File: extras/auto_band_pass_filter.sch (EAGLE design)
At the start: 31 parts, among them M1 ARDUINO-PRO-MINI-3.3V, U1 FAIRCHILD_FST3253MXFAIRCHILD_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, U2 FAIRCHILD_FST3253MXFAIRCHILD_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

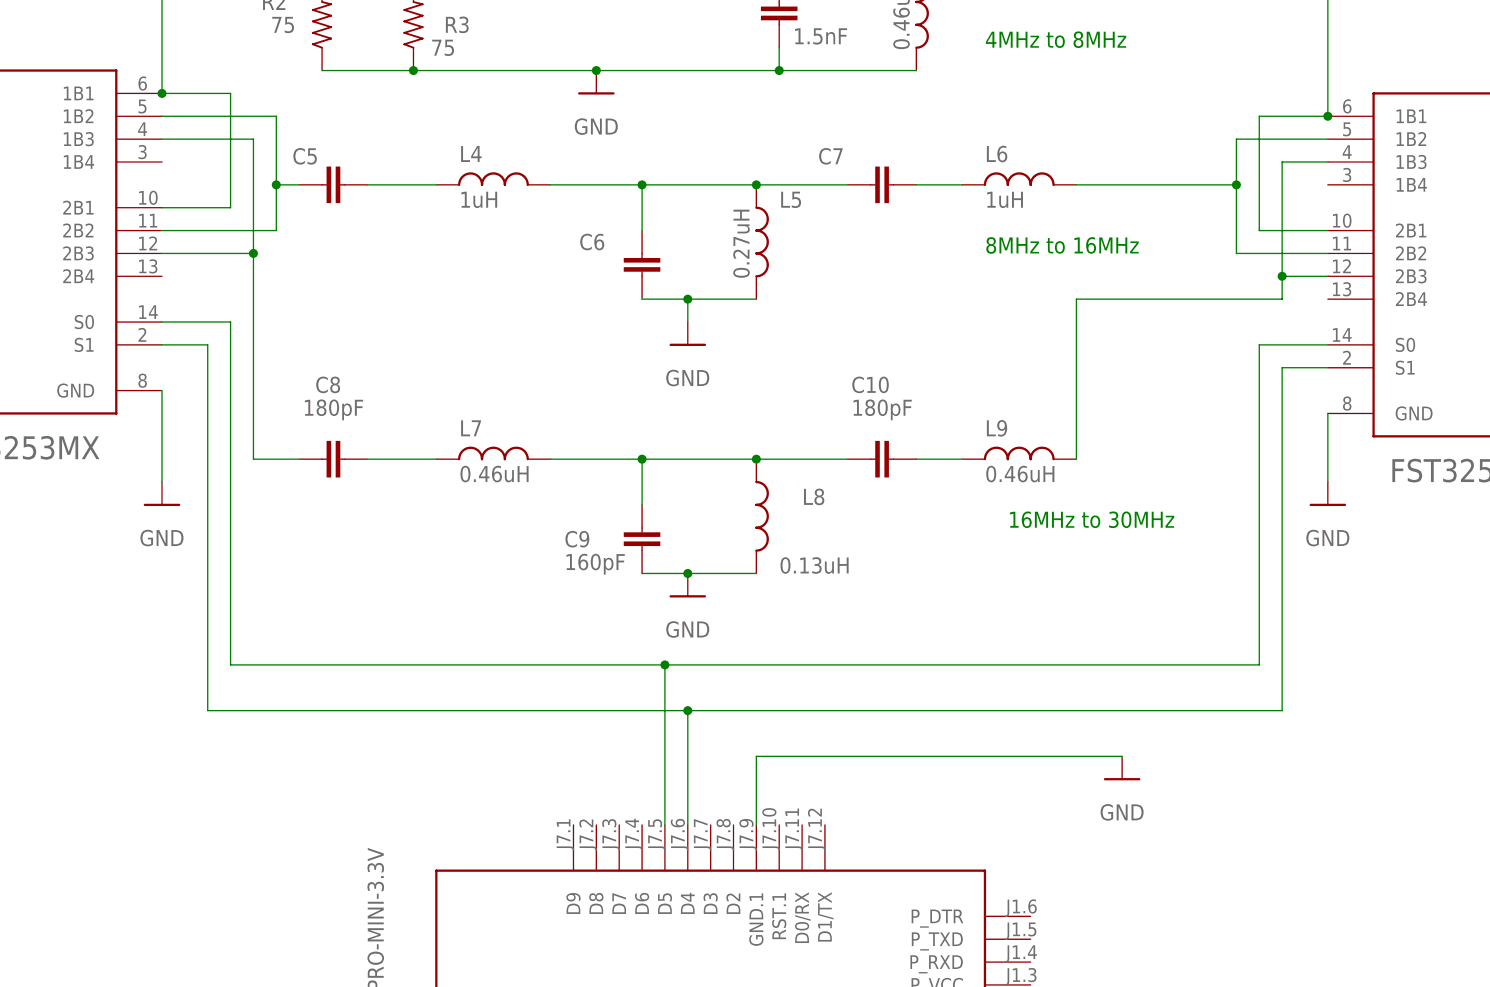
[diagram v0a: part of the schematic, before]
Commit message: Auto bandpass filter
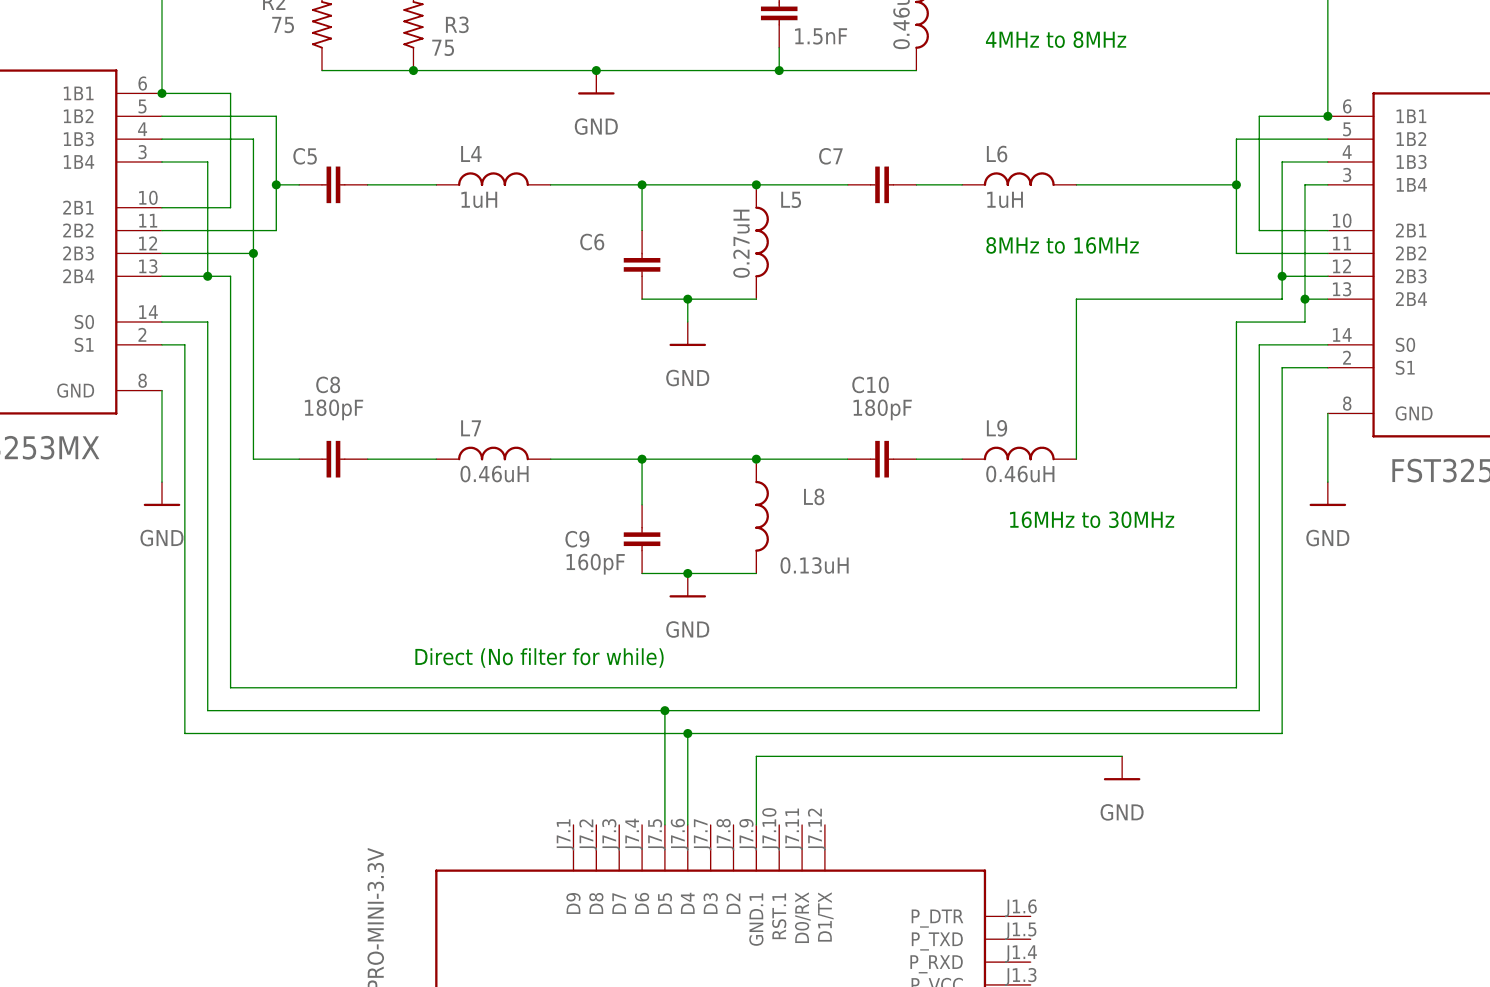
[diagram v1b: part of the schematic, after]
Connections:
- new net N$25: U1.1B4, U1.2B4, U2.1B4, U2.2B4
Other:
- note added: "Direct (No filter for while)"
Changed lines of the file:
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@@
 <text x="-139.7" y="193.04" size="1.778" layer="91">16MHz to 30MHz</text>
 <text x="-58.42" y="241.3" size="1.778" layer="91">SI4735 AMI circuit</text>
+<text x="-205.74" y="177.8" size="1.778" layer="91">Direct (No filter for while)</text>
 </plain>
 <instances>
@@
 <segment>
 <pinref part="U1" gate="G$0" pin="S0"/>
-<wire x1="-233.68" y1="215.9" x2="-226.06" y2="215.9" width="0.1524" layer="91"/>
-<wire x1="-226.06" y1="215.9" x2="-226.06" y2="177.8" width="0.1524" layer="91"/>
-<wire x1="-226.06" y1="177.8" x2="-177.8" y2="177.8" width="0.1524" layer="91"/>
-<wire x1="-177.8" y1="177.8" x2="-111.76" y2="177.8" width="0.1524" layer="91"/>
-<wire x1="-111.76" y1="177.8" x2="-111.76" y2="213.36" width="0.1524" layer="91"/>
+<wire x1="-233.68" y1="215.9" x2="-228.6" y2="215.9" width="0.1524" layer="91"/>
+<wire x1="-228.6" y1="215.9" x2="-228.6" y2="172.72" width="0.1524" layer="91"/>
+<wire x1="-228.6" y1="172.72" x2="-177.8" y2="172.72" width="0.1524" layer="91"/>
+<wire x1="-177.8" y1="172.72" x2="-111.76" y2="172.72" width="0.1524" layer="91"/>
+<wire x1="-111.76" y1="172.72" x2="-111.76" y2="213.36" width="0.1524" layer="91"/>
 <pinref part="U2" gate="G$0" pin="S0"/>
 <wire x1="-111.76" y1="213.36" x2="-104.14" y2="213.36" width="0.1524" layer="91"/>
 <pinref part="M1" gate="G$1" pin="D5"/>
-<wire x1="-177.8" y1="160.02" x2="-177.8" y2="177.8" width="0.1524" layer="91"/>
-<junction x="-177.8" y="177.8"/>
+<wire x1="-177.8" y1="160.02" x2="-177.8" y2="172.72" width="0.1524" layer="91"/>
+<junction x="-177.8" y="172.72"/>
 </segment>
 </net>
@@
 <segment>
 <pinref part="U1" gate="G$0" pin="S1"/>
-<wire x1="-233.68" y1="213.36" x2="-228.6" y2="213.36" width="0.1524" layer="91"/>
-<wire x1="-228.6" y1="213.36" x2="-228.6" y2="172.72" width="0.1524" layer="91"/>
-<wire x1="-228.6" y1="172.72" x2="-175.26" y2="172.72" width="0.1524" layer="91"/>
-<wire x1="-175.26" y1="172.72" x2="-109.22" y2="172.72" width="0.1524" layer="91"/>
-<wire x1="-109.22" y1="172.72" x2="-109.22" y2="210.82" width="0.1524" layer="91"/>
+<wire x1="-233.68" y1="213.36" x2="-231.14" y2="213.36" width="0.1524" layer="91"/>
+<wire x1="-231.14" y1="213.36" x2="-231.14" y2="170.18" width="0.1524" layer="91"/>
+<wire x1="-231.14" y1="170.18" x2="-175.26" y2="170.18" width="0.1524" layer="91"/>
+<wire x1="-175.26" y1="170.18" x2="-109.22" y2="170.18" width="0.1524" layer="91"/>
+<wire x1="-109.22" y1="170.18" x2="-109.22" y2="210.82" width="0.1524" layer="91"/>
 <pinref part="U2" gate="G$0" pin="S1"/>
 <wire x1="-109.22" y1="210.82" x2="-104.14" y2="210.82" width="0.1524" layer="91"/>
 <pinref part="M1" gate="G$1" pin="D4"/>
-<wire x1="-175.26" y1="160.02" x2="-175.26" y2="172.72" width="0.1524" layer="91"/>
-<junction x="-175.26" y="172.72"/>
+<wire x1="-175.26" y1="160.02" x2="-175.26" y2="170.18" width="0.1524" layer="91"/>
+<junction x="-175.26" y="170.18"/>
 </segment>
 </net>
@@
 </segment>
 </net>
+<net name="N$25" class="0">
+<segment>
+<pinref part="U2" gate="G$0" pin="1B4"/>
+<wire x1="-104.14" y1="231.14" x2="-106.68" y2="231.14" width="0.1524" layer="91"/>
+<wire x1="-106.68" y1="231.14" x2="-106.68" y2="218.44" width="0.1524" layer="91"/>
+<pinref part="U2" gate="G$0" pin="2B4"/>
+<wire x1="-106.68" y1="218.44" x2="-104.14" y2="218.44" width="0.1524" layer="91"/>
+<wire x1="-106.68" y1="218.44" x2="-106.68" y2="215.9" width="0.1524" layer="91"/>
+<junction x="-106.68" y="218.44"/>
+<wire x1="-106.68" y1="215.9" x2="-114.3" y2="215.9" width="0.1524" layer="91"/>
+<wire x1="-114.3" y1="215.9" x2="-114.3" y2="175.26" width="0.1524" layer="91"/>
+<wire x1="-114.3" y1="175.26" x2="-226.06" y2="175.26" width="0.1524" layer="91"/>
+<wire x1="-226.06" y1="175.26" x2="-226.06" y2="220.98" width="0.1524" layer="91"/>
+<pinref part="U1" gate="G$0" pin="1B4"/>
+<wire x1="-233.68" y1="233.68" x2="-228.6" y2="233.68" width="0.1524" layer="91"/>
+<wire x1="-228.6" y1="233.68" x2="-228.6" y2="220.98" width="0.1524" layer="91"/>
+<pinref part="U1" gate="G$0" pin="2B4"/>
+<wire x1="-228.6" y1="220.98" x2="-233.68" y2="220.98" width="0.1524" layer="91"/>
+<wire x1="-226.06" y1="220.98" x2="-228.6" y2="220.98" width="0.1524" layer="91"/>
+<junction x="-228.6" y="220.98"/>
+</segment>
+</net>

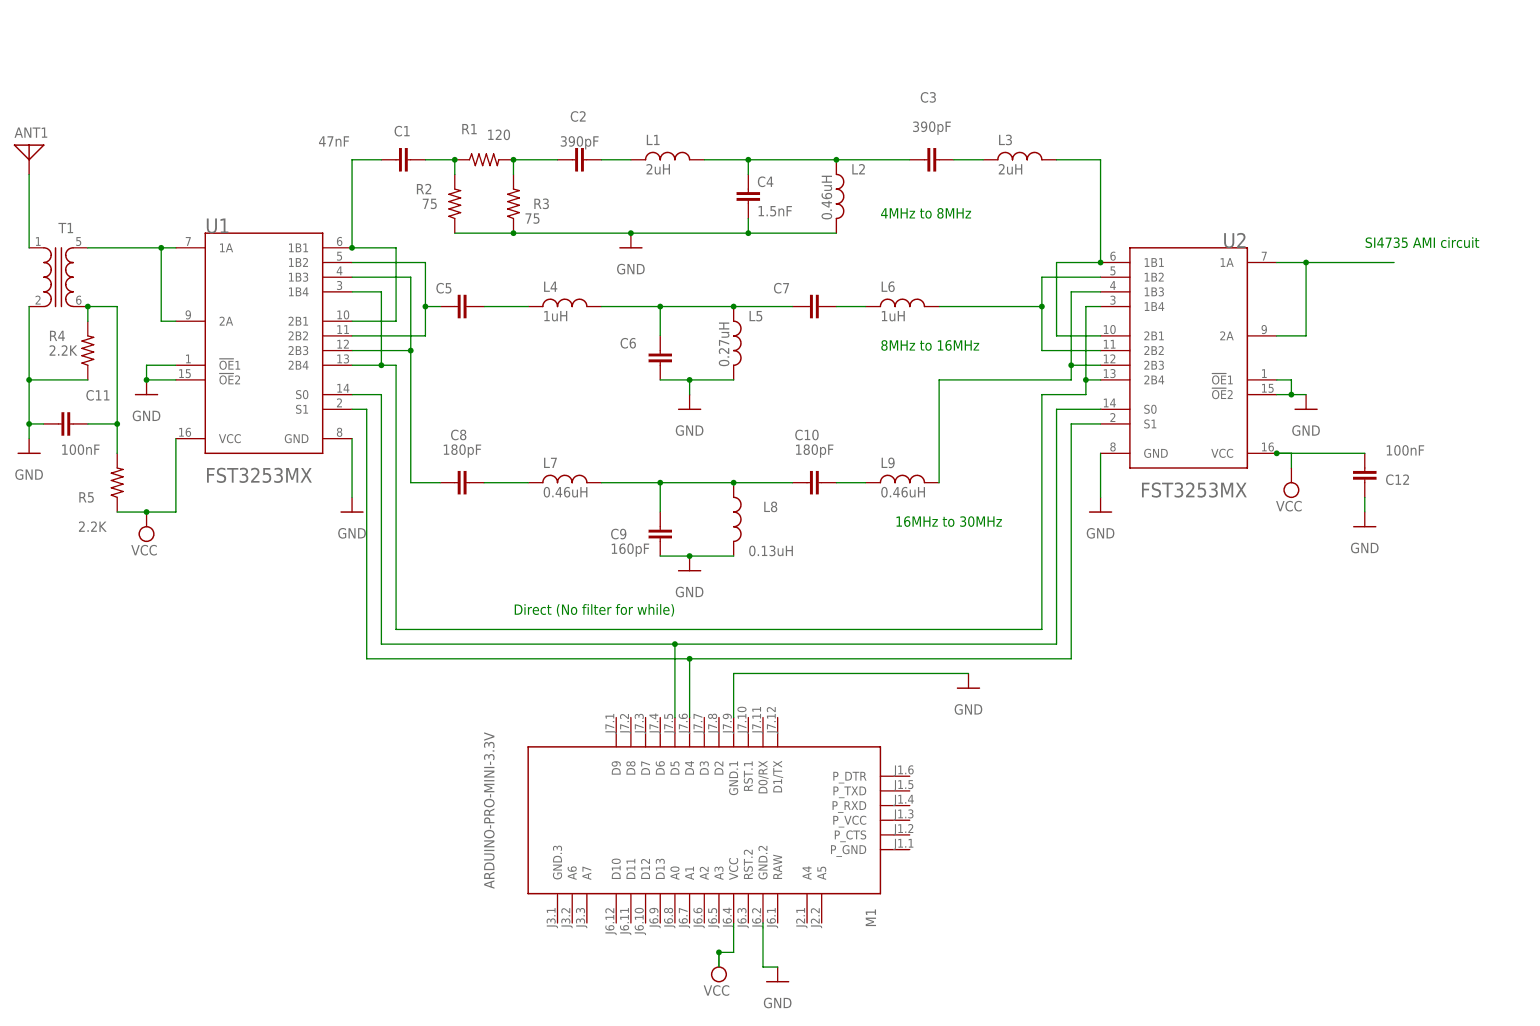
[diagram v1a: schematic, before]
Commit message: BPF controlled by Arduino
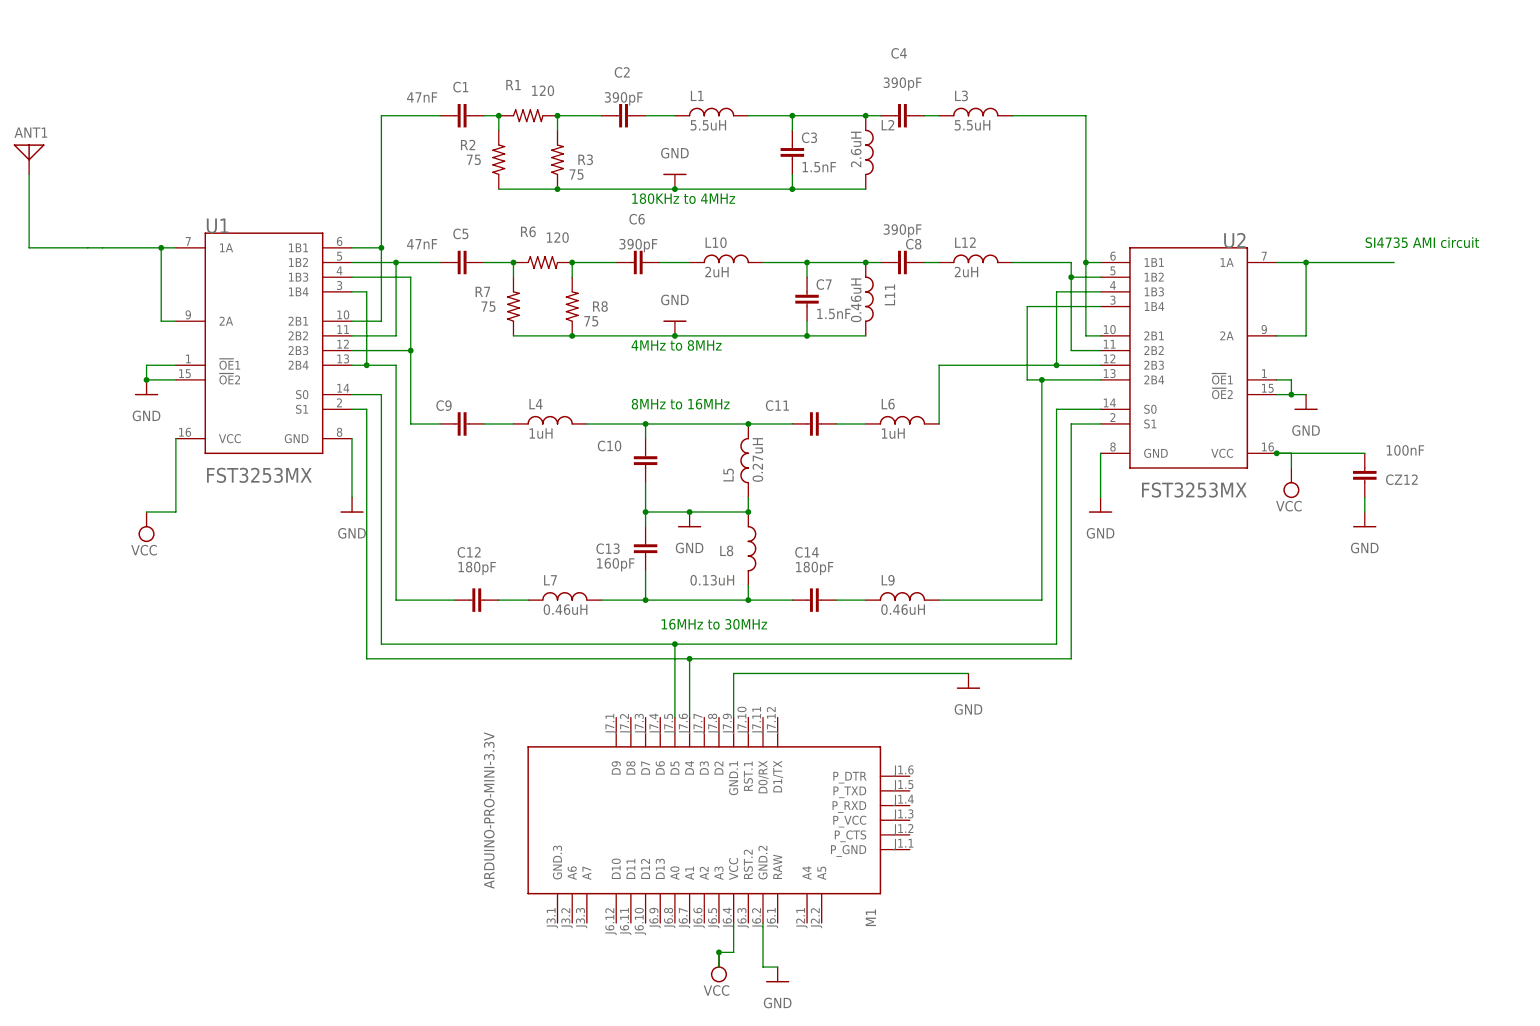
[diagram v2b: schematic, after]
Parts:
- removed R4, R5: 2.2K, Resistor:R-US_AXIAL-7.2MM-PITCH
- removed T1: (no value), special:XFORMER
- added C13: 160pF, capacitor-wima:C2,5-3
- added C14: 180pF, capacitor-wima:C2,5-3
- added CZ12: 100nF, capacitor-wima:C2,5-3
- added L10, L12: 2uH, ngspice-simulation:L
- added L11: 0.46uH, ngspice-simulation:L
- added R6: 120, Resistor:R-US_AXIAL-7.2MM-PITCH
- added R7, R8: 75, Resistor:R-US_AXIAL-7.2MM-PITCH
- C10: value 180pF -> (none)
- C11: value 100nF -> (none)
- C12: value 100nF -> 180pF
- C3: value 390pF -> 1.5nF
- C4: value 1.5nF -> 390pF
- C5: value (none) -> 47nF
- C6: value (none) -> 390pF
- C7: value (none) -> 1.5nF
- C8: value 180pF -> 390pF
- C9: value 160pF -> (none)
- L1, L3: value 2uH -> 5.5uH
- L2: value 0.46uH -> 2.6uH
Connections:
- removed net N$25: U1.1B4, U1.2B4, U2.1B4, U2.2B4
- new net N$13: C7.1, C8.1, L10.2, L11.1
- new net N$26: C6.2, L10.1
- new net N$27: L6.2, U2.1B3, U2.2B3
- new net N$28: C8.2, L12.1
- new net N$29: L9.2, U2.1B4, U2.2B4
- net GND: now also C10.1, C13.1, C3.2, C7.2, CZ12.1, L11.2, L5.1, L8.1, R7.1, R8.1; no longer C11.1, C12.1, C4.2, C6.1, C9.2, L5.2, L8.2, R4.1, T1T1.P2
- net N$10: now also C12.2; no longer C8.2
- net N$11: now also C4.2; no longer C3.2
- net N$12: now also C11.2; no longer C7.2
- net N$14: now also C9.1, U1.1B3, U1.2B3; no longer L6.2, U2.1B2, U2.2B2
- net N$16: now also C14.2; no longer C10.2
- net N$17: now also C5.2, R6.1, R7.2; no longer C8.1, U1.1B3, U1.2B3
- net N$18: now also C6.1, R6.2, R8.2; no longer L9.2, U2.1B3, U2.2B3
- net N$2: now also C9.2; no longer C5.2
- net N$20: now also ANT1.1; no longer T1T1.S1
- net N$21: now also L12.2, U2.1B2, U2.2B2; no longer ANT1.1, T1T1.P1
- net N$22: now also C12.1, U1.1B4, U1.2B4; no longer C11.2, R4.2, R5.2, T1T1.S2
- net N$4: now also C10.2, C11.1, L5.2; no longer C6.2, C7.1, L5.1
- net N$5: now also C13.2, C14.1, L8.2; no longer C10.1, C9.1, L8.1
- net VCC: now also CZ12.2; no longer C12.2, R5.1
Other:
- note added: "180KHz to 4MHz"
- note removed: "Direct (No filter for while)"
- moved on the sheet: C1, C10, C11, C12, C2, C3, C4, C5, C6, C7, C8, C9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

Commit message: ABPF
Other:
- note added: "Based on Ensemble RX II (HF/LF) Auto Band Pass Filters"
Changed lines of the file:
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@@
 <text x="-58.42" y="241.3" size="1.778" layer="91">SI4735 AMI circuit</text>
 <text x="-185.42" y="223.52" size="1.778" layer="91">4MHz to 8MHz</text>
+<text x="-284.48" y="276.86" size="1.778" layer="91">Based on Ensemble
+RX II (HF/LF) Auto Band Pass Filters</text>
 </plain>
 <instances>
@@
 </drawing>
 <compatibility>
+<note version="6.3" minversion="6.2.2" severity="warning">
+Since Version 6.2.2 text objects can contain more than one line,
+which will not be processed correctly with this version.
+</note>
 <note version="8.2" severity="warning">
 Since Version 8.2, EAGLE supports online libraries. The ids

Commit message: ABPF
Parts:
- L10, L12: value 2uH -> 0.46uH
- L11: value 0.46uH -> 0.13uH
- L4, L6: value 1uH -> 2uH
- L5: value 0.27uH -> 0.46uH
- L7, L9: value 0.46uH -> 1uH
- L8: value 0.13uH -> 0.27uH
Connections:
- net GND: now also L11.1, L5.2; no longer L11.2, L5.1
- net N$10: now also L10.1; no longer L7.1
- net N$12: now also L9.1; no longer L6.1
- net N$13: now also L4.2, L5.1; no longer L10.2, L11.1
- net N$16: now also L12.1; no longer L9.1
- net N$2: now also L7.1; no longer L4.1
- net N$21: now also L6.2; no longer L12.2
- net N$26: now also L4.1; no longer L10.1
- net N$27: now also L9.2; no longer L6.2
- net N$28: now also L6.1; no longer L12.1
- net N$29: now also L12.2; no longer L9.2
- net N$4: now also L7.2, L8.2; no longer L4.2, L5.2
- net N$5: now also L10.2, L11.2; no longer L7.2, L8.2
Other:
- moved on the sheet: L10, L11, L12, L4, L5, L6, L7, L8, L9
